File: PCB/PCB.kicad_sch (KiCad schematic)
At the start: 10 parts, among them J1 Conn_01x02, J2 Conn_01x02, SW1 SW_MEC_5E, SW2 SW_MEC_5E, SW3 SW_MEC_5E, SW4 SW_DPDT_x2, U1 ESP32-c3, U2 MPU6050_PCB

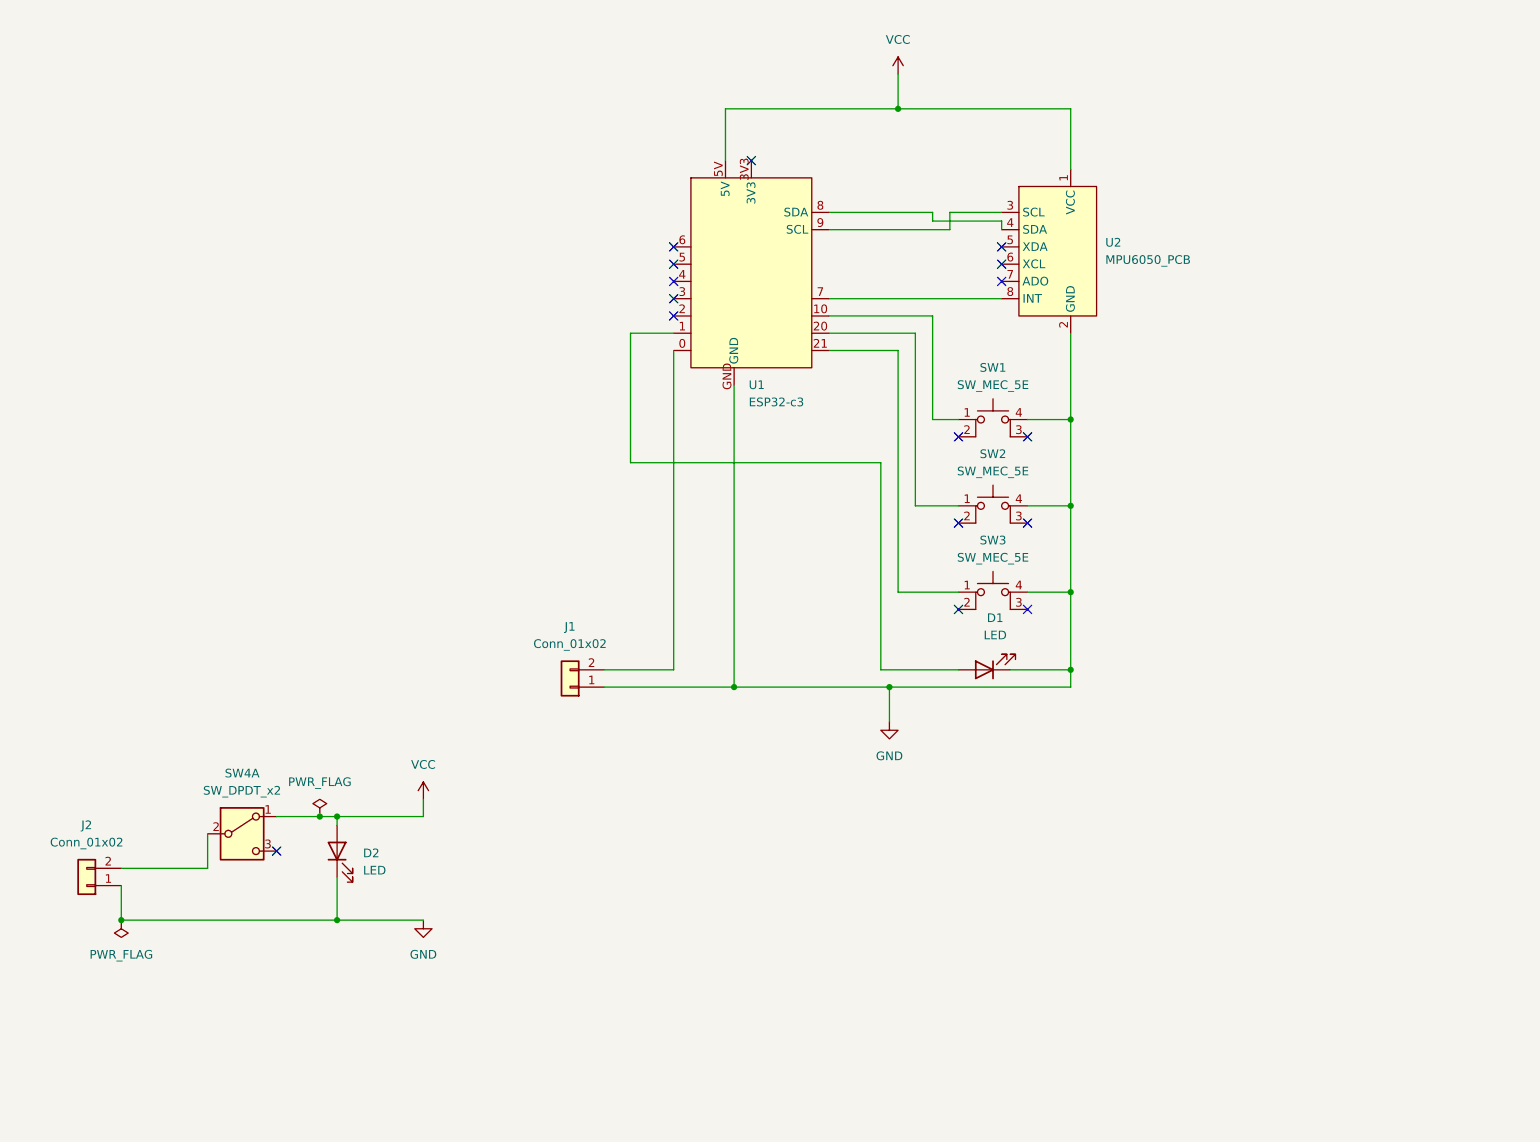
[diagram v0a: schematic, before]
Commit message: feat: zaverecna zprava, pcb m2 WIP
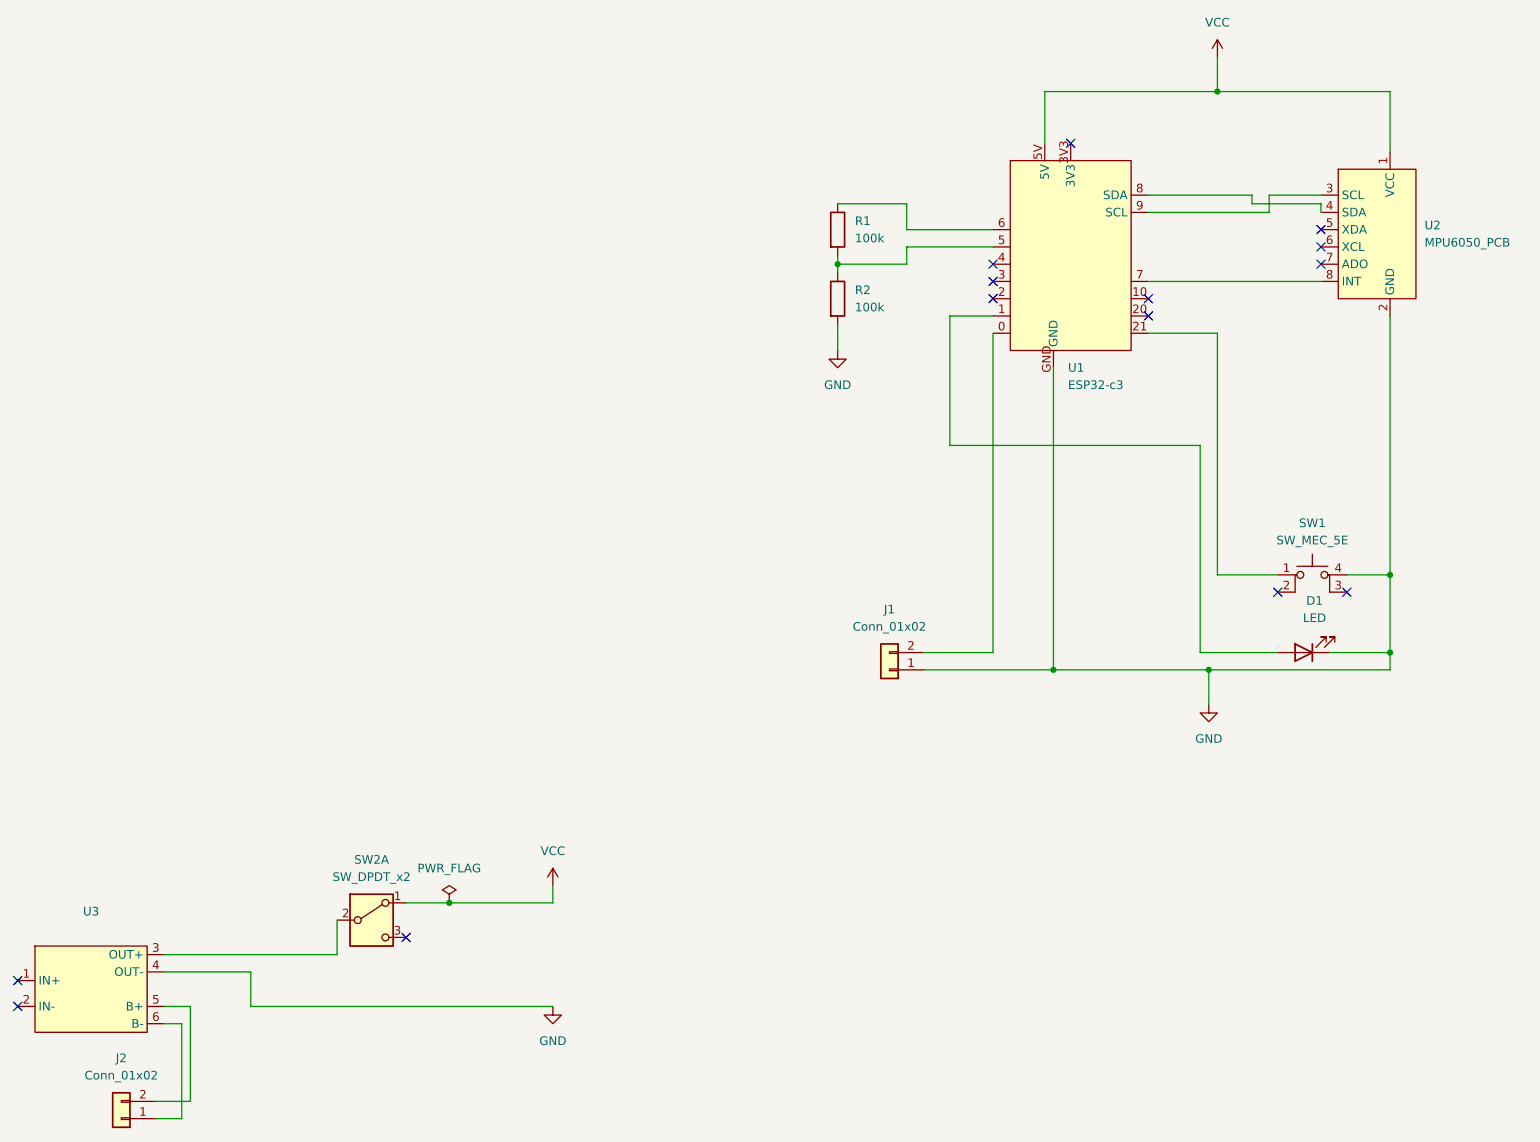
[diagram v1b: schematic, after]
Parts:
- removed D2: LED, LED_THT:LED_Oval_W5.2mm_H3.8mm, symbol Device:LED
- removed SW1, SW2: SW_MEC_5E, Tlacitka:Arduino_tlacitko, symbol Switch:SW_MEC_5E
- added R1, R2: 100k, Resistor_THT:R_Axial_DIN0207_L6.3mm_D2.5mm_P7.62mm_Horizontal, symbol Device:R
- added U3: ~, nabijecky_moje_pcb:TP4056, symbol TP4056_moje:TP4056
- renumbered SW3 to SW1, SW4 to SW2
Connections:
- net GND: now also R2.2, U3.4 (OUT-); no longer J2.1 (Pin_1)
- net at U1.5: now also R1.2, R2.1
- net at U1.6: now also R1.1
- net at SW2.2 (B): now also U3.3 (OUT+); no longer J2.2 (Pin_2)
- new net: J2.2 (Pin_2), U3.5 (B+)
- new net: J2.1 (Pin_1), U3.6 (B-)
- no-connect marks 16 -> 14
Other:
- moved on the sheet: D1, J1, J2, SW1, SW2A, U1, U2
